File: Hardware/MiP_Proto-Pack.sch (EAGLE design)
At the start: 5 parts

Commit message: fixed labels
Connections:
- net N$1 renamed 6V
- net N$2 renamed TX
- net N$3 renamed RX
- net N$4 renamed GND
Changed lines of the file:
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@@
 </busses>
 <nets>
-<net name="N$1" class="0">
+<net name="6V" class="0">
 <segment>
 <pinref part="JP11" gate="G$1" pin="1"/>
@@
 </segment>
 </net>
-<net name="N$2" class="0">
+<net name="TX" class="0">
 <segment>
 <pinref part="JP11" gate="G$1" pin="2"/>
@@
 </segment>
 </net>
-<net name="N$3" class="0">
+<net name="RX" class="0">
 <segment>
 <pinref part="JP11" gate="G$1" pin="3"/>
@@
 </segment>
 </net>
-<net name="N$4" class="0">
+<net name="GND" class="0">
 <segment>
 <pinref part="JP11" gate="G$1" pin="4"/>

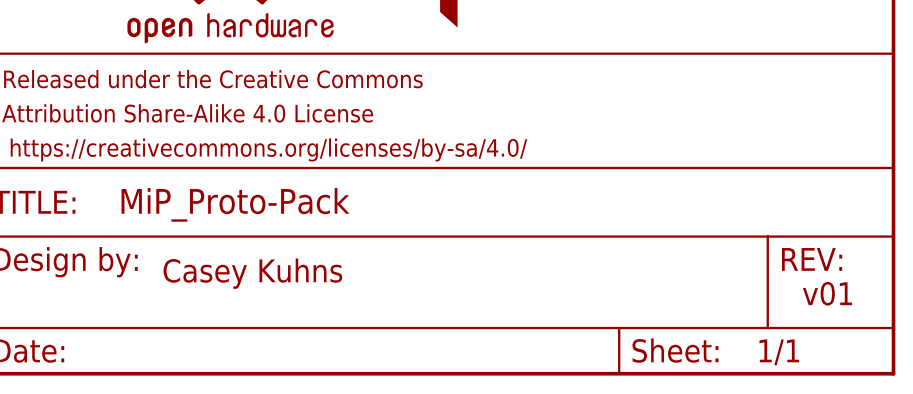
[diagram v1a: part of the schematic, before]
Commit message: corrected version number, added name to back of PCB
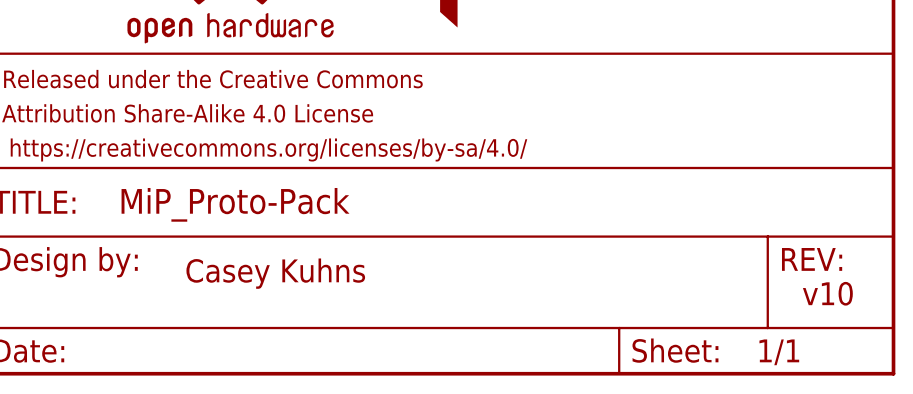
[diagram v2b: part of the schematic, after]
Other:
- note added: "v10"
- note removed: "v01"
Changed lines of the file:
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@@
 <sheet>
 <plain>
-<text x="167.64" y="10.16" size="2.54" layer="94">Casey Kuhns</text>
-<text x="238.76" y="7.62" size="2.54" layer="94">v01</text>
+<text x="170.18" y="10.16" size="2.54" layer="94">Casey Kuhns</text>
+<text x="238.76" y="7.62" size="2.54" layer="94">v10</text>
 </plain>
 <instances>
